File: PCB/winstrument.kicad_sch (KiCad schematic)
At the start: 105 parts, among them J1 Conn_01x05_Pin, J2 Conn_01x03_Pin, J3 Conn_02x04_Odd_Even, J4 RS422, J5 Conn_01x09_Pin, J6 Conn_01x02_Pin, J7 ICSP, Q1 2N7002, Q2 2N7002, U1 NCP662SQ50, U11 TXB0104D, U12 TCAN337, U13 INA326, U14 INA326, U2 TLV75533PDBV, U3 TPS5430DDA, U4 STM32L552CETx, U7 ST232ExD, U8 TPS27SA08CPWPR, U9 ADM3488ExR

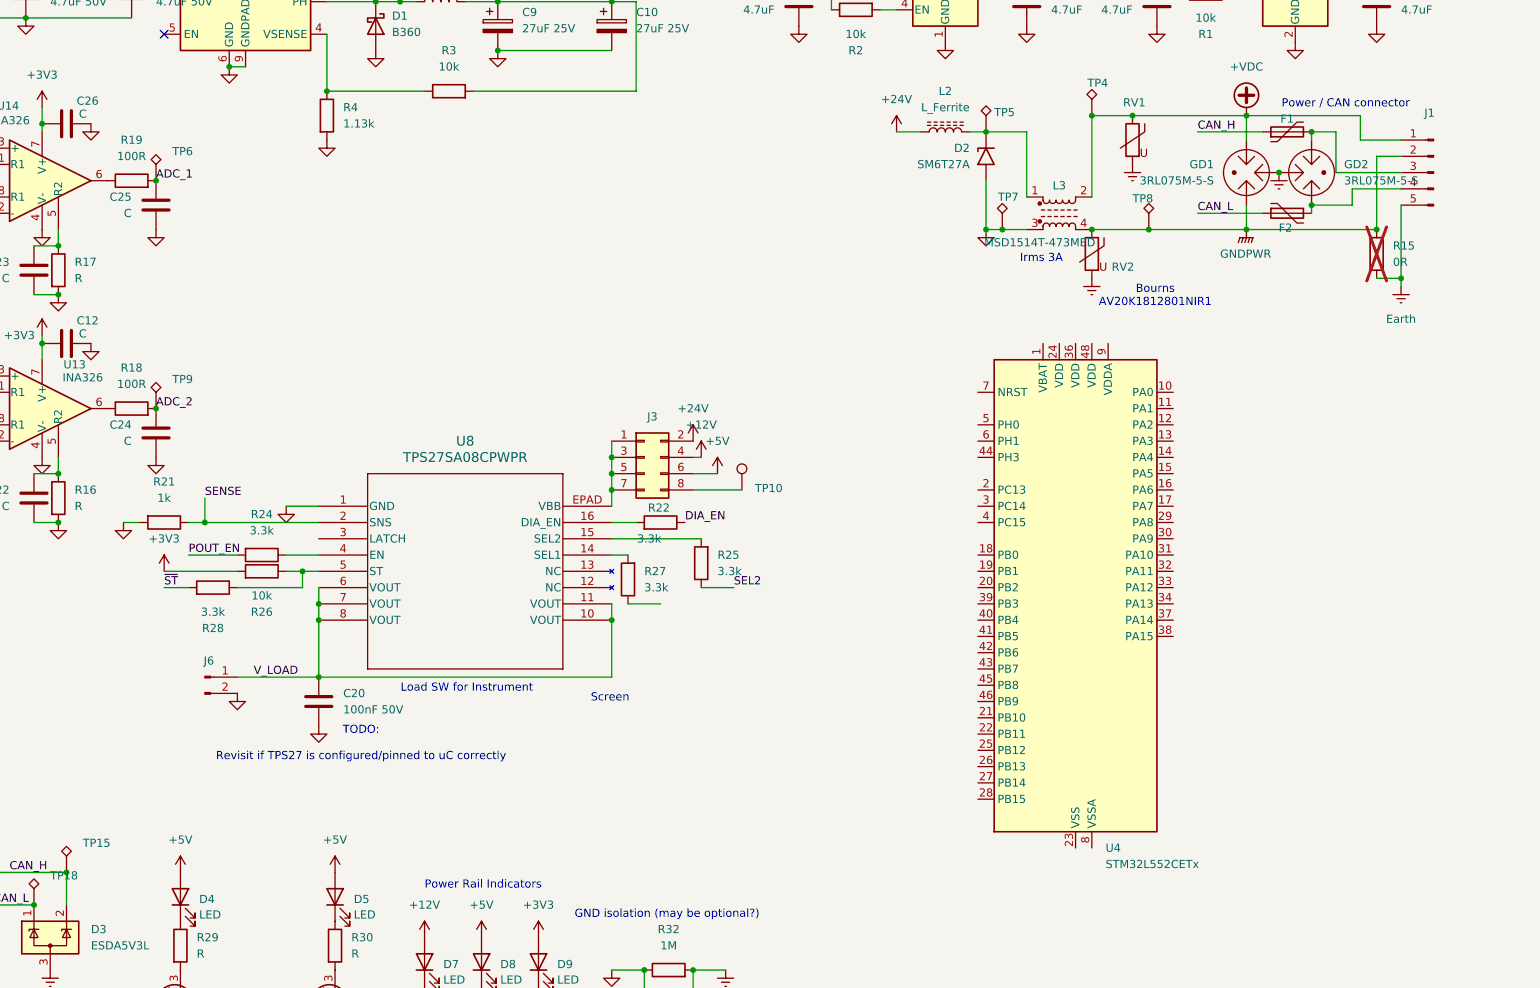
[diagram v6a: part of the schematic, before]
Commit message: committing leftovers from the past, prior to modifying PCBs for optoisolators
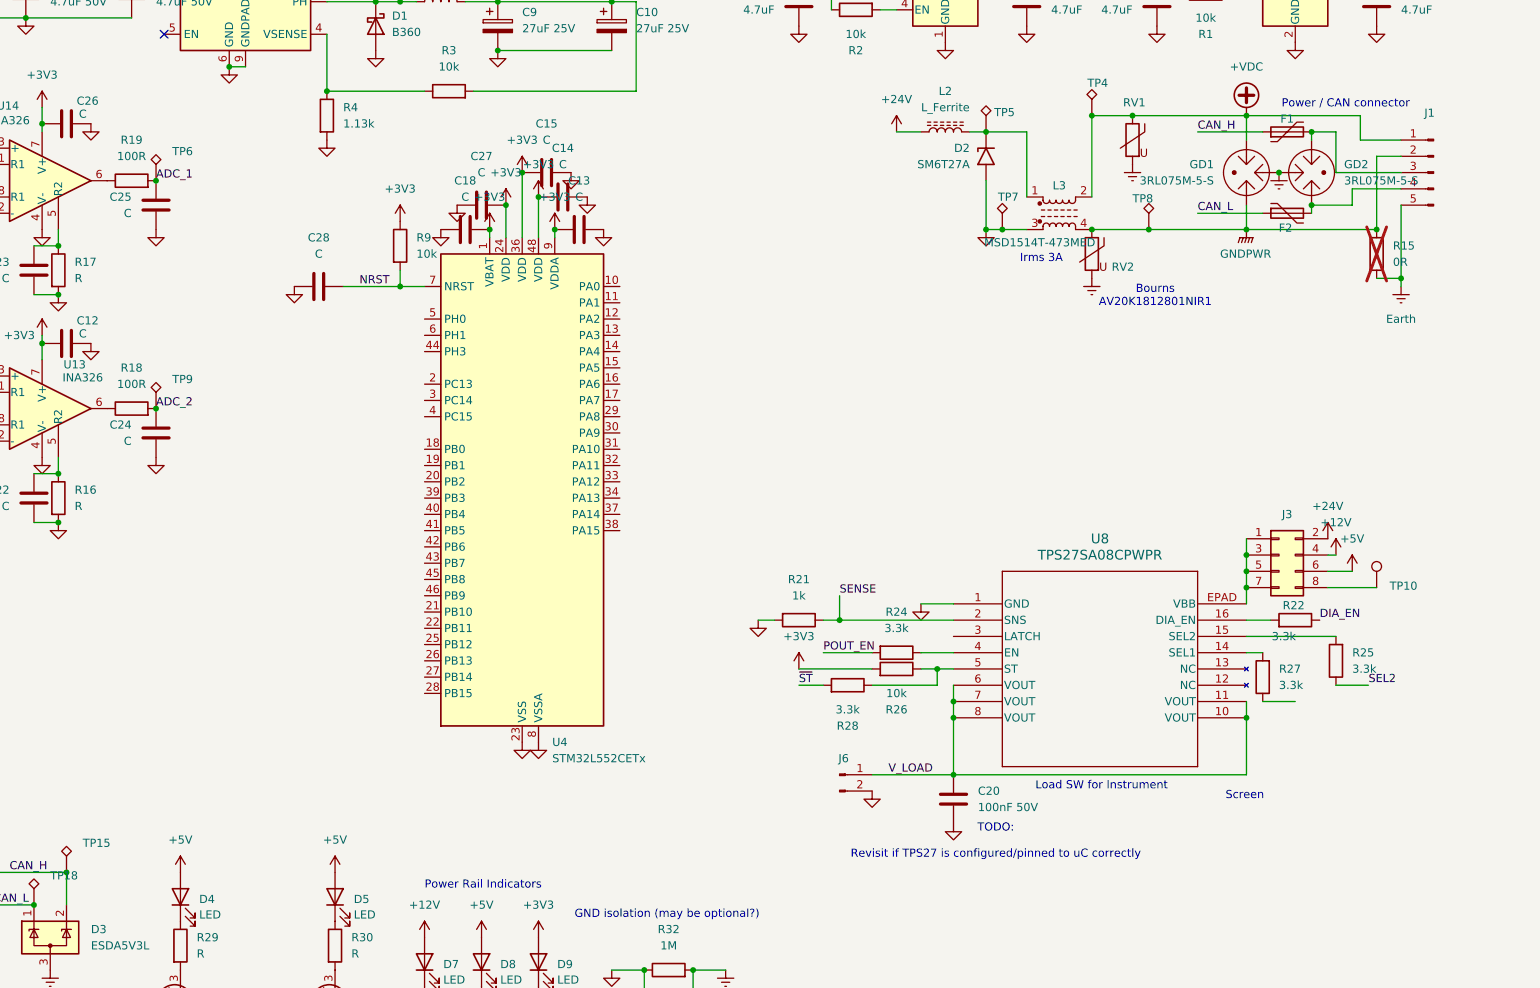
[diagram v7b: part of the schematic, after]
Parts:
- added C13, C14, C15, C18, C27, C28: C, symbol Device:C
- added R9: 10k, symbol Device:R
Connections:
- net +3V3: now also U4.1 (VBAT), U4.24 (VDD), U4.36 (VDD), U4.48 (VDD), U4.9 (VDDA), C13.1, C14.1, C15.1, C18.2, C27.2, R9.1
- net GND: now also U4.23 (VSS), U4.35 (VSS), U4.47 (VSS), U4.8 (VSSA), C13.2, C14.2, C15.2, C18.1, C27.1, C28.1
- net NRST: now also U4.7 (NRST), C28.2, R9.2
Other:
- moved on the sheet: C20, J3, J6, R21, R22, R24, R25, R26, R27, R28, TP10, U4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
